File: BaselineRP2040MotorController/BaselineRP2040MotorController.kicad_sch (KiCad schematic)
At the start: 2 parts, among them J1 To UC, J4 XT60 Power Connector

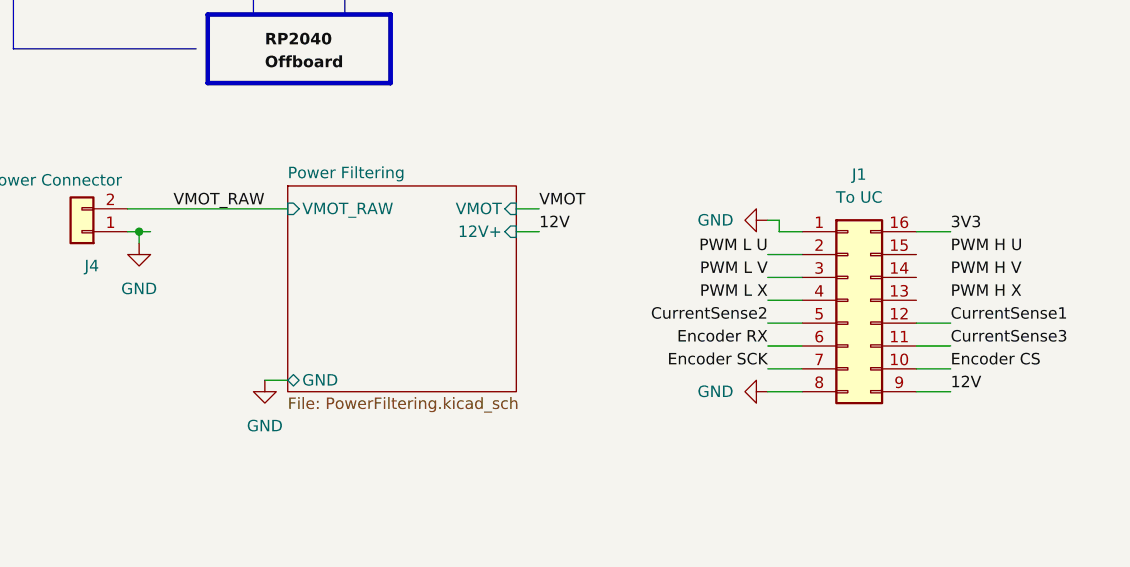
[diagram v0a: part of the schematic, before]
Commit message: Should have been a 4 layer board.
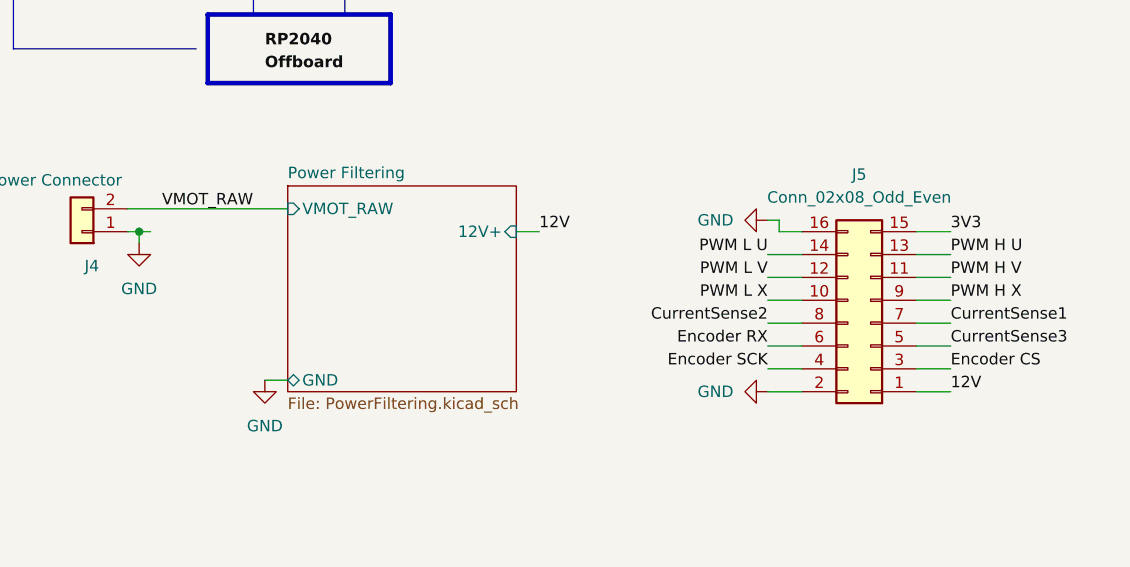
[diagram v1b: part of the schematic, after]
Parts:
- removed J1: To UC, symbol Connector_Generic:Conn_02x08_Counter_Clockwise
- added J5: Conn_02x08_Odd_Even, Connector_PinHeader_2.54mm:PinHeader_2x08_P2.54mm_Horizontal, symbol Connector_Generic:Conn_02x08_Odd_Even
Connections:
- net 12V: now also J5.1 (Pin_1)
- net 3V3: now also J5.15 (Pin_15)
- net CurrentSense1: now also J5.7 (Pin_7)
- net CurrentSense2: now also J5.8 (Pin_8)
- net CurrentSense3: now also J5.5 (Pin_5)
- net Encoder CS: now also J5.3 (Pin_3)
- net Encoder RX: now also J5.6 (Pin_6)
- net Encoder SCK: now also J5.4 (Pin_4)
- net GND: now also J5.16 (Pin_16), J5.2 (Pin_2)
- net PWM H U: now also J5.13 (Pin_13)
- net PWM H V: now also J5.11 (Pin_11)
- net PWM H X: now also J5.9 (Pin_9)
- net PWM L U: now also J5.14 (Pin_14)
- net PWM L V: now also J5.12 (Pin_12)
- net PWM L X: now also J5.10 (Pin_10)
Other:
- sheet Power Filtering ports: added none; removed VMOT
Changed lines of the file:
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@@
+	(wire
+		(pts
+			(xy 133.35 86.36) (xy 137.16 86.36)
+		)
+		(stroke
+			(width 0)
+			(type default)
+		)
+	)
 	(wire
 		(pts
@@
 	(wire
 		(pts
-			(xy 88.9 76.2) (xy 91.44 76.2)
-		)
-		(stroke
-			(width 0)
-			(type default)
-		)
-	)
-	(wire
-		(pts
 			(xy 133.35 93.98) (xy 137.16 93.98)
 		)
@@
 	(wire
 		(pts
+			(xy 133.35 81.28) (xy 137.16 81.28)
+		)
+		(stroke
+			(width 0)
+			(type default)
+		)
+	)
+	(wire
+		(pts
 			(xy 173.99 140.97) (xy 173.99 146.05)
 		)
@@
 		(pts
 			(xy 167.64 92.71) (xy 171.45 92.71)
+		)
+		(stroke
+			(width 0)
+			(type default)
+		)
+	)
+	(wire
+		(pts
+			(xy 137.16 83.82) (xy 133.35 83.82)
 		)
 		(stroke
@@
 	)
 	(label "VMOT_RAW"
-		(at 50.8 76.2 0)
+		(at 49.53 76.2 0)
 		(fields_autoplaced yes)
 		(effects
@@
 				(thickness 0.254)
 				(bold yes)
-			)
-			(justify left bottom)
-		)
-	)
-	(label "VMOT"
-		(at 91.44 76.2 0)
-		(fields_autoplaced yes)
-		(effects
-			(font
-				(size 1.27 1.27)
 			)
 			(justify left bottom)
@@
 	)
 	(symbol
-		(lib_id "Connector_Generic:Conn_02x08_Counter_Clockwise")
-		(at 125.73 86.36 0)
-		(unit 1)
-		(exclude_from_sim no)
-		(in_bom yes)
-		(on_board yes)
-		(dnp no)
-		(fields_autoplaced yes)
-		(property "Reference" "J1"
-			(at 127 72.39 0)
-			(effects
-				(font
-					(size 1.27 1.27)
-				)
-			)
-		)
-		(property "Value" "To UC"
-			(at 127 74.93 0)
-			(effects
-				(font
-					(size 1.27 1.27)
-				)
-			)
-		)
-		(property "Footprint" ""
-			(at 125.73 86.36 0)
-			(effects
-				(font
-					(size 1.27 1.27)
-				)
-				(hide yes)
-			)
-		)
-		(property "Datasheet" "~"
-			(at 125.73 86.36 0)
-			(effects
-				(font
-					(size 1.27 1.27)
-				)
-				(hide yes)
-			)
-		)
-		(property "Description" "Generic connector, double row, 02x08, counter clockwise pin numbering scheme (similar to DIP package numbering), script generated (kicad-library-utils/schlib/autogen/connector/)"
-			(at 125.73 86.36 0)
-			(effects
-				(font
-					(size 1.27 1.27)
-				)
-				(hide yes)
-			)
-		)
-		(pin "1"
-		)
-		(pin "5"
-		)
-		(pin "6"
-		)
-		(pin "7"
-		)
-		(pin "8"
-		)
-		(pin "16"
-		)
-		(pin "9"
-		)
-		(pin "10"
-		)
-		(pin "11"
-		)
-		(pin "13"
-		)
-		(pin "12"
-		)
-		(pin "2"
-		)
-		(pin "14"
-		)
-		(pin "3"
-		)
-		(pin "4"
-		)
-		(pin "15"
-		)
-		(instances
-			(project "BaselineRP2040MotorController"
-				(path "/085e5f08-c826-4caa-b8e2-0a741609456e"
-					(reference "J1")
-					(unit 1)
-				)
-			)
-		)
-	)
-	(symbol
 		(lib_id "Connector_Generic:Conn_01x02")
 		(at 40.64 78.74 180)
@@
 		)
 	)
+	(symbol
+		(lib_id "Connector_Generic:Conn_02x08_Odd_Even")
+		(at 128.27 88.9 180)
+		(unit 1)
+		(exclude_from_sim no)
+		(in_bom yes)
+		(on_board yes)
+		(dnp no)
+		(fields_autoplaced yes)
+		(property "Reference" "J5"
+			(at 127 72.39 0)
+			(effects
+				(font
+					(size 1.27 1.27)
+				)
+			)
+		)
+		(property "Value" "Conn_02x08_Odd_Even"
+			(at 127 74.93 0)
+			(effects
+				(font
+					(size 1.27 1.27)
+				)
+			)
+		)
+		(property "Footprint" "Connector_PinHeader_2.54mm:PinHeader_2x08_P2.54mm_Horizontal"
+			(at 128.27 88.9 0)
+			(effects
+				(font
+					(size 1.27 1.27)
+				)
+				(hide yes)
+			)
+		)
+		(property "Datasheet" "~"
+			(at 128.27 88.9 0)
+			(effects
+				(font
+					(size 1.27 1.27)
+				)
+				(hide yes)
+			)
+		)
+		(property "Description" "Generic connector, double row, 02x08, odd/even pin numbering scheme (row 1 odd numbers, row 2 even numbers), script generated (kicad-library-utils/schlib/autogen/connector/)"
+			(at 128.27 88.9 0)
+			(effects
+				(font
+					(size 1.27 1.27)
+				)
+				(hide yes)
+			)
+		)
+		(pin "12"
+		)
+		(pin "10"
+		)
+		(pin "16"
+		)
+		(pin "4"
+		)
+		(pin "8"
+		)
+		(pin "3"
+		)
+		(pin "6"
+		)
+		(pin "1"
+		)
+		(pin "13"
+		)
+		(pin "5"
+		)
+		(pin "2"
+		)
+		(pin "15"
+		)
+		(pin "9"
+		)
+		(pin "14"
+		)
+		(pin "7"
+		)
+		(pin "11"
+		)
+		(instances
+			(project "BaselineRP2040MotorController"
+				(path "/085e5f08-c826-4caa-b8e2-0a741609456e"
+					(reference "J5")
+					(unit 1)
+				)
+			)
+		)
+	)
 	(sheet
 		(at 176.53 128.27)
@@
 			)
 		)
-		(pin "VMOT" input
-			(at 88.9 76.2 0)
-			(effects
-				(font
-					(size 1.27 1.27)
-				)
-				(justify right)
-			)
-		)

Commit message: MinMax
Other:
- removed sheet Hall Effect Encoders
- sheet BLDC Power Control ports: added none; removed U_SENSE, V_SENSE, X_SENSE

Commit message: Heh - Super cut down.
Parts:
- removed J5: Conn_02x08_Odd_Even, Connector_PinHeader_2.54mm:PinHeader_2x08_P2.54mm_Horizontal, symbol Connector_Generic:Conn_02x08_Odd_Even
- added J1: Conn_01x08, Connector_JST:JST_PH_S8B-PH-K_1x08_P2.00mm_Horizontal, symbol Connector_Generic:Conn_01x08
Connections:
- net 12V: now also J1.1 (Pin_1)
- net GND: now also J1.8 (Pin_8)
- net PWM H U: now also J1.2 (Pin_2)
- net PWM H V: now also J1.4 (Pin_4)
- net PWM H X: now also J1.6 (Pin_6)
- net PWM L U: now also J1.3 (Pin_3)
- net PWM L V: now also J1.5 (Pin_5)
- net PWM L X: now also J1.7 (Pin_7)
